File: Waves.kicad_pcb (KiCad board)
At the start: 4 copper layers, 49.8 x 106.5 mm, 151 parts, among them J1 AudioJack2_SwitchT, J10 AudioJack2_SwitchT, J11 Conn_01x04_Male, J12 Conn_01x04_Male, J13 AudioJack2_SwitchT, J14 AudioJack2_SwitchT, J15 Conn_02x05_Odd_Even, J2 AudioJack2_SwitchT, J3 AudioJack2_SwitchT, J4 AudioJack2_SwitchT, J5 AudioJack2_SwitchT, J6 AudioJack2_SwitchT, J7 AudioJack2_SwitchT, J8 AudioJack2_SwitchT, J9 AudioJack2_SwitchT, Q1 BC847, Q2 BC847, Q3 BC847, Q4 BC847, Q5 BC847, Q6 BC847, SW1 SW_Push, SW2 Rotary_Encoder_Switch, SW3 SW_Push_LED, SW4 SW_Push_LED, SW5 SW_Push_LED, SW6 SW_Push_LED, U1 STM32G431, U2 AT25xxx, U3 IPS240x240, U4 PCM5100, U5 TL072, U6 R-78E3.3-0.5, U7 LD2981ABU33TR, U8 MCP6004, U9 MCP6004, Y1 8MHz

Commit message: Pre-routing state.
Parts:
- moved C43 0.25 mm to (109.0, 134.6)
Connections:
- J10 pad TN: +3V3 -> +3.3VA
- J9 pad TN: +3V3 -> +3.3VA
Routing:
- added copper zone on In1.Cu, net +3.3VA
- added copper zone on In1.Cu, net +3V3
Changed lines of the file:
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@@
   (layers
     (0 F.Cu signal)
-    (1 In1.Cu mixed)
-    (2 In2.Cu power)
+    (1 In1.Cu power)
+    (2 In2.Cu power hide)
     (31 B.Cu signal)
     (32 B.Adhes user)
@@
       (net 75 GND))
     (pad TN thru_hole oval (at 0 3.38) (size 2.6 1.6) (drill oval 1.6 0.6) (layers *.Cu *.Mask)
-      (net 76 +3V3))
+      (net 4 +3.3VA))
     (model ${KIPRJMOD}/Local.pretty/PJ398SM.step
       (offset (xyz 0 0 9))
@@
       (net 75 GND))
     (pad TN thru_hole oval (at 0 3.38) (size 2.6 1.6) (drill oval 1.6 0.6) (layers *.Cu *.Mask)
-      (net 76 +3V3))
+      (net 4 +3.3VA))
     (model ${KIPRJMOD}/Local.pretty/PJ398SM.step
       (offset (xyz 0 0 9))
@@
     )
   )
-  (module Local:PJ398SM (layer F.Cu)
+  (module Local:PJ398SM locked (layer F.Cu)
     (at 109.1184 121.92)
     (fp_text reference J1 (at 0 -6.9) (layer F.SilkS)
@@
   )
   (module Capacitor_SMD:C_0603_1608Metric (layer B.Cu)
-    (at 109.22 134.62 180)
+    (at 108.966 134.62 180)
     (descr "Capacitor SMD 0603 (1608 Metric), square (rectangular) end terminal, IPC_7351 nominal, (Body size source: http://www.tortai-tech.com/upload/download/2011102023233369053.pdf), generated with kicad-footprint-generator")
     (tags capacitor)
@@
       )
     )
+  )
+  (zone (net 4) (net_name +3.3VA) (layer In1.Cu) (hatch edge 0.508)
+    (connect_pads (clearance 0.508))
+    (min_thickness 0.254)
+    (fill yes (arc_segments 32) (thermal_gap 0.508) (thermal_bridge_width 0.508))
+    (polygon
+      (pts
+        (xy 144.7165 151.765) (xy 109.093 151.765) (xy 109.093 114.427) (xy 120.904 114.427) (xy 120.904 121.92)
+        (xy 132.715 121.92) (xy 132.842 114.427) (xy 144.5895 114.427)
+      )
+    )
+  )
+  (zone (net 76) (net_name +3V3) (layer In1.Cu) (hatch edge 0.508)
+    (connect_pads (clearance 0.508))
+    (min_thickness 0.254)
+    (fill yes (arc_segments 32) (thermal_gap 0.508) (thermal_bridge_width 0.508))
+    (polygon
+      (pts
+        (xy 101.981 48.387) (xy 101.981 113.919) (xy 151.765 113.919) (xy 151.765 48.387)
+      )
+    )

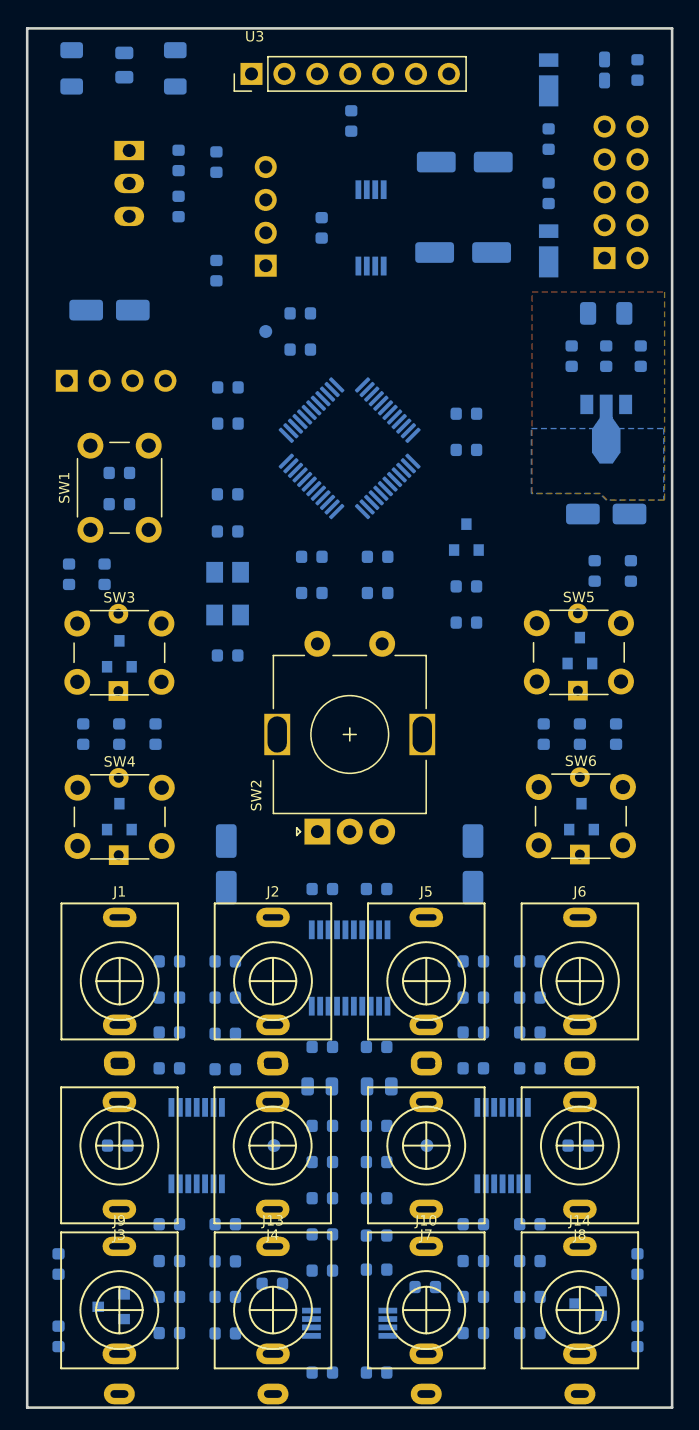
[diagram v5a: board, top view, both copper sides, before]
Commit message: Improved placement and avoidance of criss-crossing.
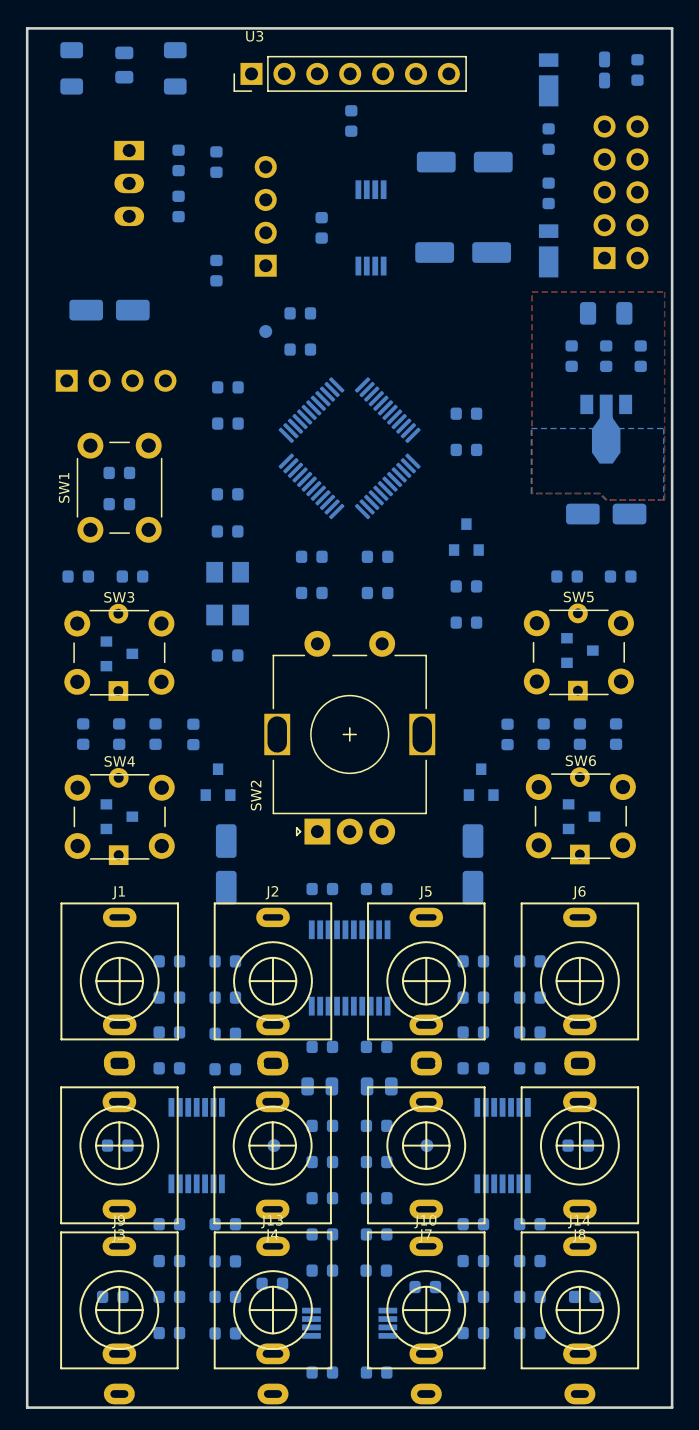
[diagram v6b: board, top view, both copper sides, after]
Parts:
- moved R24 47.6 mm to (114.8, 102.9), turned to 270 degrees
- moved R21 47.6 mm to (139.1, 102.9), turned to 270 degrees
- moved Q3 41.3 mm to (116.7, 106.6), turned to 90 degrees
- moved Q1 41.1 mm to (137.0, 106.6), turned to 90 degrees
- moved R15 11.2 mm to (128.9, 144.3)
- moved R11 11.1 mm to (129.0, 133.1)
- moved C26 5.68 mm to (129.0, 135.9)
- moved C30 5.59 mm to (129.0, 141.5)
- moved R23 4.90 mm to (108.6, 146.3), turned to 180 degrees
- moved R20 4.79 mm to (145.0, 146.3), turned to 0 degrees
- moved R26 2.18 mm to (143.7, 90.7), turned to 180 degrees
- moved R22 2.17 mm to (110.1, 90.7), turned to 180 degrees
- moved R8 0.90 mm to (147.8, 90.7), turned to 0 degrees
- moved R1 0.73 mm to (105.9, 90.7), turned to 0 degrees
- turned D3 to 270 degrees
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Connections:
- C46 pad 1: CV3A -> CV4A
- C47 pad 1: CV4A -> CV3A
- C51 pad 1: CV3B -> CV4B
- C52 pad 1: CV4B -> CV3B
- R34 pad 2: /QuadCV/CV2 -> /QuadCV/CV3
- R36 pad 2: /QuadCV/CV3 -> /QuadCV/CV2
- R37 pad 1: CV3A -> CV4A
- R38 pad 1: CV4A -> CV3A
- R46 pad 2: /sheet5E1FC1E7/CV2 -> /sheet5E1FC1E7/CV3
- R48 pad 2: /sheet5E1FC1E7/CV3 -> /sheet5E1FC1E7/CV2
- R49 pad 1: CV3B -> CV4B
- R50 pad 1: CV4B -> CV3B
- U8 pad 14: CV4A -> CV3A
- U8 pad 8: CV3A -> CV4A
- U9 pad 14: CV4B -> CV3B
- U9 pad 8: CV3B -> CV4B

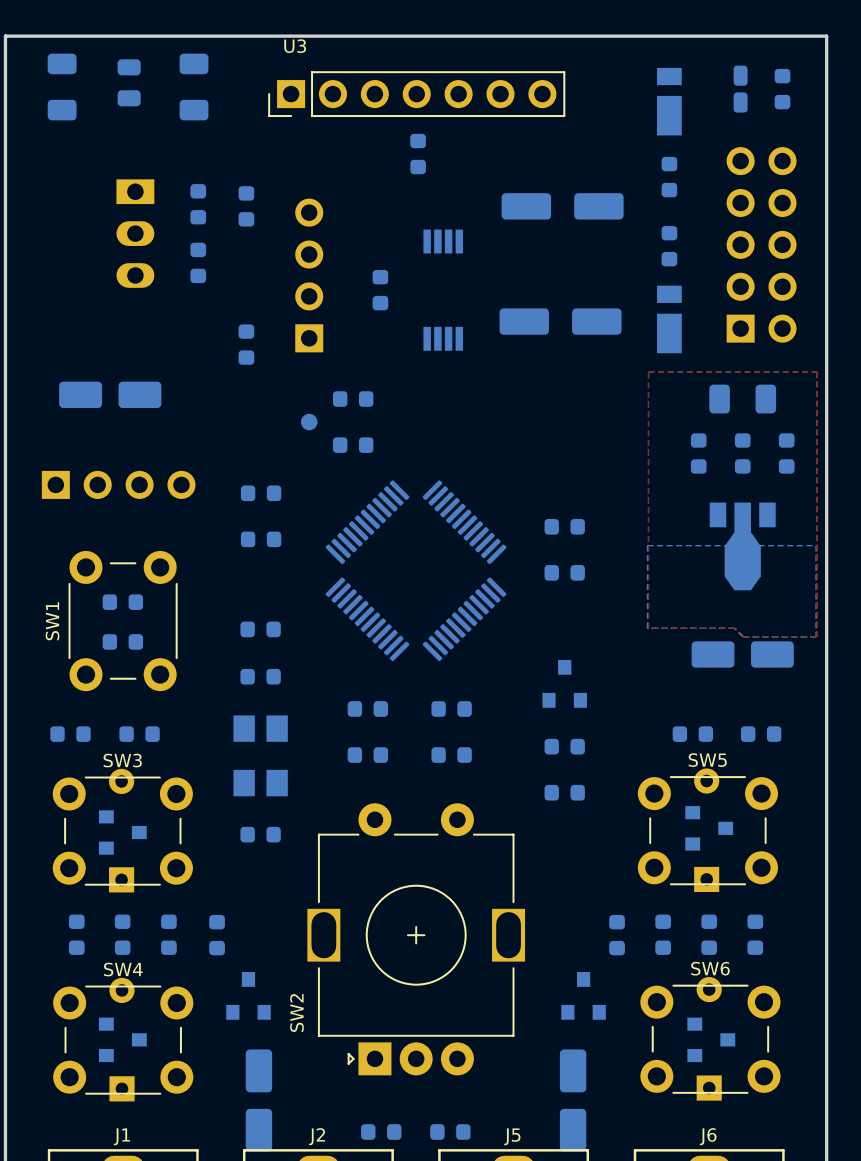
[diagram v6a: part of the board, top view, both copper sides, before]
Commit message: Power layer adjustments.
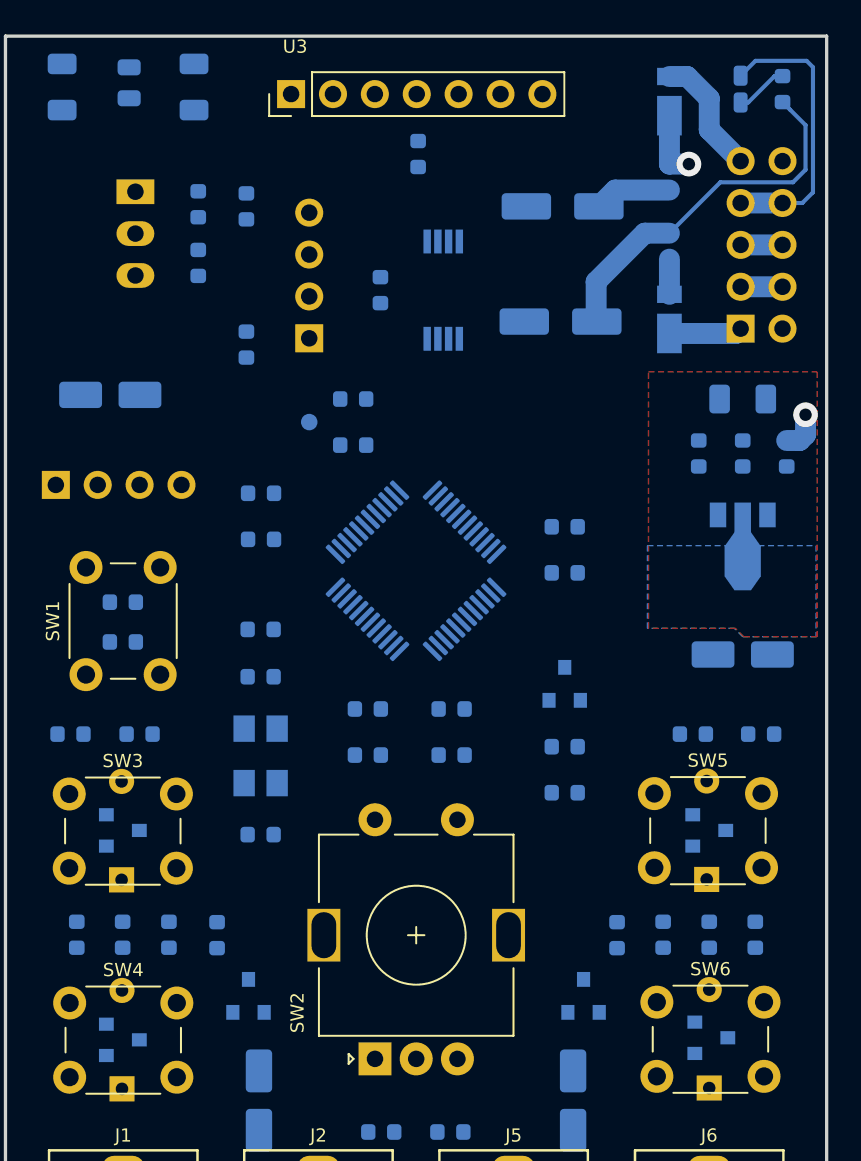
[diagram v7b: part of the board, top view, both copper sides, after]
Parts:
- moved Q2 0.13 mm to (109.1, 96.5)
- moved Q5 0.13 mm to (144.7, 96.5)
- moved Q6 0.13 mm to (144.8, 109.1)
- turned D3 to 90 degrees
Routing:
- net Net-(C31-Pad1): track 0.00 -> 25.9 mm, vias 0 -> 2
- net -12V: track 0.00 -> 22.6 mm
- net GND: track 0.00 -> 22.2 mm
- net Net-(D1-Pad2): track 0.00 -> 10.1 mm
- net Net-(D2-Pad1): track 0.00 -> 6.98 mm
- net +12V: track 0.00 -> 4.69 mm
- net Net-(D3-Pad1): track 0.00 -> 3.20 mm
- net Net-(D2-Pad2): track 0.00 -> 2.13 mm
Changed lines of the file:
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@@
     (thickness 1.6)
     (drawings 75)
-    (tracks 0)
+    (tracks 45)
     (zones 0)
     (modules 151)
@@
   (setup
     (last_trace_width 0.25)
+    (user_trace_width 0.635)
+    (user_trace_width 1.27)
+    (user_trace_width 1.905)
+    (user_trace_width 2.54)
     (trace_clearance 0.2)
     (zone_clearance 0.508)
@@
     (via_min_size 0.4)
     (via_min_drill 0.3)
+    (user_via 1 0.5)
+    (user_via 1.5 0.75)
+    (user_via 2 1)
     (uvia_size 0.3)
     (uvia_drill 0.1)
@@
   )
   (module Package_TO_SOT_SMD:SOT-23 (layer B.Cu)
-    (at 144.78 109.22)
+    (at 144.78 109.093)
     (descr "SOT-23, Standard")
     (tags SOT-23)
@@
   )
   (module Package_TO_SOT_SMD:SOT-23 (layer B.Cu)
-    (at 144.653 96.393)
+    (at 144.653 96.52)
     (descr "SOT-23, Standard")
     (tags SOT-23)
@@
   )
   (module Package_TO_SOT_SMD:SOT-23 (layer B.Cu)
-    (at 109.093 96.647)
+    (at 109.093 96.52)
     (descr "SOT-23, Standard")
     (tags SOT-23)
@@
   )
   (module LED_SMD:LED_0603_1608Metric_Castellated placed (layer B.Cu)
-    (at 146.558 51.562 270)
+    (at 146.558 51.562 90)
     (descr "LED SMD 0603 (1608 Metric), castellated end terminal, IPC_7351 nominal, (Body size source: http://www.tortai-tech.com/upload/download/2011102023233369053.pdf), generated with kicad-footprint-generator")
     (tags "LED castellated")
@@
     (fp_line (start -0.5 0.4) (end -0.8 0.1) (layer B.Fab) (width 0.1))
     (fp_line (start 0.8 0.4) (end -0.5 0.4) (layer B.Fab) (width 0.1))
-    (pad 2 smd roundrect (at 0.8125 0 270) (size 1.225 0.85) (layers B.Cu B.Paste B.Mask) (roundrect_rratio 0.25)
+    (pad 2 smd roundrect (at 0.8125 0 90) (size 1.225 0.85) (layers B.Cu B.Paste B.Mask) (roundrect_rratio 0.25)
       (net 75 GND))
-    (pad 1 smd roundrect (at -0.8125 0 270) (size 1.225 0.85) (layers B.Cu B.Paste B.Mask) (roundrect_rratio 0.25)
+    (pad 1 smd roundrect (at -0.8125 0 90) (size 1.225 0.85) (layers B.Cu B.Paste B.Mask) (roundrect_rratio 0.25)
       (net 27 "Net-(D3-Pad1)"))
     (model ${KISYS3DMOD}/LED_SMD.3dshapes/LED_0603_1608Metric_Castellated.wrl
@@
   (gr_line (start 151.775 154.849999) (end 151.775 48.349999) (layer Edge.Cuts) (width 0.2))
   (gr_line (start 101.974999 154.849999) (end 151.775 154.849999) (layer Edge.Cuts) (width 0.2))
+  (segment (start 138.9535 57.6835) (end 137.963 58.674) (width 1.27) (layer B.Cu) (net 8))
+  (segment (start 142.24 57.6835) (end 138.9535 57.6835) (width 1.27) (layer B.Cu) (net 8))
+  (segment (start 137.795 65.618) (end 137.836 65.659) (width 1.27) (layer B.Cu) (net 9))
+  (segment (start 137.795 63.246) (end 137.795 65.618) (width 1.27) (layer B.Cu) (net 9))
+  (segment (start 142.24 60.2995) (end 140.7415 60.2995) (width 1.27) (layer B.Cu) (net 9))
+  (segment (start 140.7415 60.2995) (end 137.795 63.246) (width 1.27) (layer B.Cu) (net 9))
+  (segment (start 150.495 56.4515) (end 150.495 53.7465) (width 0.25) (layer B.Cu) (net 9))
+  (segment (start 145.326 57.2135) (end 149.733 57.2135) (width 0.25) (layer B.Cu) (net 9))
+  (segment (start 142.24 60.2995) (end 145.326 57.2135) (width 0.25) (layer B.Cu) (net 9))
+  (segment (start 149.559612 52.811112) (end 149.098 52.3495) (width 0.25) (layer B.Cu) (net 9))
+  (segment (start 150.495 53.7465) (end 149.559612 52.811112) (width 0.25) (layer B.Cu) (net 9))
+  (segment (start 149.733 57.2135) (end 150.495 56.4515) (width 0.25) (layer B.Cu) (net 9))
+  (segment (start 149.098 55.929) (end 146.558 55.929) (width 1.905) (layer In1.Cu) (net 24))
+  (segment (start 144.653 54.024) (end 146.558 55.929) (width 1.27) (layer B.Cu) (net 24))
+  (segment (start 144.653 52.133998) (end 144.653 54.024) (width 1.27) (layer B.Cu) (net 24))
+  (segment (start 142.24 50.799) (end 143.318002 50.799) (width 1.27) (layer B.Cu) (net 24))
+  (segment (start 143.318002 50.799) (end 144.653 52.133998) (width 1.27) (layer B.Cu) (net 24))
+  (segment (start 142.24 61.8745) (end 142.24 64.007) (width 1.27) (layer B.Cu) (net 25))
+  (segment (start 149.098 66.089) (end 146.558 66.089) (width 1.905) (layer In1.Cu) (net 26))
+  (segment (start 146.265 66.382) (end 146.558 66.089) (width 1.27) (layer B.Cu) (net 26))
+  (segment (start 142.24 66.382) (end 146.265 66.382) (width 1.27) (layer B.Cu) (net 26))
+  (segment (start 148.6155 50.7745) (end 149.098 50.7745) (width 0.25) (layer B.Cu) (net 27))
+  (segment (start 146.558 52.3745) (end 147.0155 52.3745) (width 0.25) (layer B.Cu) (net 27))
+  (segment (start 147.0155 52.3745) (end 148.6155 50.7745) (width 0.25) (layer B.Cu) (net 27))
+  (segment (start 146.558 58.469) (end 149.098 58.469) (width 1.27) (layer B.Cu) (net 75))
+  (segment (start 146.558 61.009) (end 149.098 61.009) (width 1.27) (layer B.Cu) (net 75))
+  (segment (start 146.558 63.549) (end 149.098 63.549) (width 1.27) (layer B.Cu) (net 75))
+  (segment (start 150.300081 58.469) (end 149.098 58.469) (width 0.25) (layer B.Cu) (net 75))
+  (segment (start 150.945011 57.82407) (end 150.300081 58.469) (width 0.25) (layer B.Cu) (net 75))
+  (segment (start 150.945011 50.234011) (end 150.945011 57.82407) (width 0.25) (layer B.Cu) (net 75))
+  (segment (start 150.5585 49.8475) (end 150.945011 50.234011) (width 0.25) (layer B.Cu) (net 75))
+  (segment (start 146.558 50.7495) (end 147.46 49.8475) (width 0.25) (layer B.Cu) (net 75))
+  (segment (start 147.46 49.8475) (end 150.5585 49.8475) (width 0.25) (layer B.Cu) (net 75))
+  (segment (start 142.24 56.1085) (end 142.24 53.174) (width 1.27) (layer B.Cu) (net 88))
+  (segment (start 149.352 72.8725) (end 150.1395 72.8725) (width 1.27) (layer B.Cu) (net 88))
+  (segment (start 150.1395 72.8725) (end 150.495 72.517) (width 1.27) (layer B.Cu) (net 88))
+  (via (at 150.495 71.3105) (size 1.5) (drill 0.75) (layers F.Cu B.Cu) (net 88))
+  (segment (start 150.495 72.517) (end 150.495 71.3105) (width 1.27) (layer B.Cu) (net 88))
+  (segment (start 142.24 56.1085) (end 143.421 56.1085) (width 1.27) (layer B.Cu) (net 88))
+  (via (at 143.421 56.1085) (size 1.5) (drill 0.75) (layers F.Cu B.Cu) (net 88))
+  (segment (start 149.479 70.2945) (end 150.495 71.3105) (width 1.27) (layer In1.Cu) (net 88))
+  (segment (start 147.560498 70.2945) (end 149.479 70.2945) (width 1.27) (layer In1.Cu) (net 88))
+  (segment (start 144.145 66.879002) (end 147.560498 70.2945) (width 1.27) (layer In1.Cu) (net 88))
+  (segment (start 143.421 56.1085) (end 144.145 56.8325) (width 1.27) (layer In1.Cu) (net 88))
+  (segment (start 144.145 56.8325) (end 144.145 66.879002) (width 1.27) (layer In1.Cu) (net 88))
   (zone (net 75) (net_name GND) (layer In2.Cu) (hatch edge 0.508)
     (connect_pads (clearance 0.508))
@@
   )
   (zone (net 75) (net_name GND) (layer B.Cu) (hatch edge 0.508)
-    (connect_pads (clearance 0.508))
+    (connect_pads no (clearance 0.508))
     (min_thickness 0.254)
     (fill yes (arc_segments 32) (thermal_gap 0.508) (thermal_bridge_width 0.508))
@@
     (polygon
       (pts
-        (xy 144.7165 151.765) (xy 109.093 151.765) (xy 109.093 114.427) (xy 120.904 114.427) (xy 120.904 121.92)
-        (xy 132.715 121.92) (xy 132.842 114.427) (xy 144.5895 114.427)
+        (xy 151.79675 154.813) (xy 101.94925 154.813) (xy 101.981 113.284) (xy 120.015 113.284) (xy 120.015 121.92)
+        (xy 133.858 121.92) (xy 133.858 113.411) (xy 151.7015 113.411)
+      )
+    )
+  )
+  (zone (net 76) (net_name +3V3) (layer In1.Cu) (hatch edge 0.508)
+    (connect_pads (clearance 0.508))
+    (min_thickness 0.254)
+    (fill yes (arc_segments 32) (thermal_gap 0.508) (thermal_bridge_width 0.508))
+    (polygon
+      (pts
+        (xy 121.412 111.887) (xy 121.412 121.285) (xy 132.207 121.285) (xy 132.207 111.887)
       )
     )
@@
     (polygon
       (pts
-        (xy 101.981 48.387) (xy 101.981 113.919) (xy 151.765 113.919) (xy 151.765 48.387)
+        (xy 135.763 68.072) (xy 139.319 68.072) (xy 139.319 111.76) (xy 101.981 111.76) (xy 101.981 48.387)
+        (xy 135.763 48.387)
+      )
+    )
+  )
+  (zone (net 4) (net_name +3.3VA) (layer In1.Cu) (hatch edge 0.508)
+    (connect_pads (clearance 0.508))
+    (min_thickness 0.254)
+    (fill yes (arc_segments 32) (thermal_gap 0.508) (thermal_bridge_width 0.508))
+    (polygon
+      (pts
+        (xy 151.765 72.136) (xy 141.097 72.136) (xy 141.097 115.316) (xy 151.765 115.316)
       )
     )
